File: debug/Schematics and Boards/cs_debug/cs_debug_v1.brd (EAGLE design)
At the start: 38.1 x 44.5 mm, 186 parts, among them J1 J-JTAG-CORTEX_SMD, J19 Solar, J2 J-JTAG-CORTEX_SMD, J3 J-JTAG-CORTEX-NEEDLE6-LEGS, J4 J-SERIAL-PORT, J5 J-WURTH-USBC, Q10 2N7002P, Q3 FDN340P, Q4 2N7002P, Q5 FDN340P, Q6 2N7002P, Q7 FDN340P, Q8 2N7002P, Q9 FDN340P, U1 AP2120N-3.3TRG1, U10 OPA357AIDBVTG4, U11 DAC7574IDGS, U12 MCP73871T-2CCI/ML, U13 USB2412-DZK, U2 TLV1117LV33DCYR, U3 INA225AIDGK, U4 OPA357AIDBVTG4, U5 INA225AIDGK, U6 OPA357AIDBVTG4, U7 INA225AIDGK, U8 OPA357AIDBVTG4, U9 INA225AIDGK, Y1 HCM49-24.000MABJ-UT, Y101 32.768kHz, Y102 12mHz-12pF-K7

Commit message: Add and name test points for debug board
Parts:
- removed C4: 68p, Capacitors:C0402
- removed C5, C6: 0.1u, Capacitors:C0402
- removed R10, R12, R14: 10k, Resistors:R0402
- removed R11: 100k, Resistors:R0402
- removed R13, R9: 249k, Resistors:R0402
- removed R15: 5.1, Resistors:R0603
- removed U3: INA225AIDGK, Amplifiers:DGK-MSOP8_INA225
- removed U4: OPA357AIDBVTG4, Amplifiers:OPA357AIDBVTG4
- added C20: 680pF, Capacitors:C0402
- added C21, C45: 0.1u, Capacitors:C0402
- added R53, R55, R57: 10k, Resistors:R0402
- added R54: 100k, Resistors:R0402
- added R56: 249k, Resistors:R0402
- added R58, R59: 5.1, Resistors:R0603
- added TP_3V3_IPROC, TP_3V3_MEAS, TP_M_D_DA_VO, TP_M_D_OA_EN, TP_M_D_OA_N, TP_M_D_OA_P, TP_M_D_OA_VO, TP_M_D_SDN, TP_M_D_VN, TP_M_D_VOI, TP_M_P_DA_VO, TP_M_P_OA_N, TP_M_P_OA_P, TP_M_P_OA_VO, TP_M_P_SDN, TP_M_P_VN, TP_M_P_VOI, TP_M_S_DA_VO, TP_M_S_OA_EN, TP_M_S_OA_N, TP_M_S_OA_P, TP_M_S_OA_VO, TP_M_S_SDN, TP_M_S_VN, TP_M_S_VOI, TP_M_T_DA_VO, TP_M_T_OA_EN, TP_M_T_OA_N, TP_M_T_OA_P, TP_M_T_OA_VO, TP_M_T_SDN, TP_M_T_VN, TP_M_T_VOI, TP_SCL, TP_SDA, T_M_P_OA_EN: TPTP10SQ, TestPoints:TP10SQ
- added U14: INA225AIDGK, Amplifiers:DGK-MSOP8_INA225
- added U15: OPA357AIDBVTG4, Amplifiers:OPA357AIDBVTG4
- C10, C13, C7: value 68p -> 680pF
- R16, R24, R40: value 5.1 -> 249k; device Resistors:R0603 -> Resistors:R0402
- R17, R21, R33, R37: value 249k -> 10k
- R18, R34: value 10k -> 100k
- R19, R35: value 100k -> 10k
- R20, R36: value 10k -> 249k
- R22, R38: value 10k -> 5.1; device Resistors:R0402 -> Resistors:R0603
- moved Q3 134.9 mm to (88.9, -91.4), turned to 180 degrees
- moved R16 126.5 mm to (96.5, -90.8), turned to 180 degrees
- moved Q4 125.1 mm to (88.9, -86.4), turned to 270 degrees
- moved Q7 88.0 mm to (88.9, -67.3), turned to 180 degrees
- moved R31 85.9 mm to (101.6, -67.3)
- moved U7 85.8 mm to (101.6, -62.2), turned to 270 degrees
- moved U5 85.2 mm to (101.6, -86.4), turned to 270 degrees
- moved R22 80.1 mm to (101.6, -91.4)
- moved C10 80.0 mm to (105.4, -62.2), turned to 90 degrees
- moved R25 79.6 mm to (96.5, -66.7), turned to 180 degrees
- moved C7 79.4 mm to (105.4, -86.4), turned to 90 degrees
- moved Q8 78.5 mm to (88.9, -62.2), turned to 270 degrees
- moved U8 78.5 mm to (94.0, -63.5), turned to 90 degrees
- moved U6 78.0 mm to (94.0, -87.6), turned to 90 degrees
- moved R17 77.8 mm to (94.0, -90.8)
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- renumbered JP11 to JP_VREG_SEL
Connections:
- net CM_DTR_DIFFAMP_N3 renamed CM_DIFFAMP_N3
- net CM_DTR_DIFFAMP_P3 renamed CM_DIFFAMP_P3
- removed net CM_DTR_OPAMP_ENABLE3: Q7.G, Q8.D, R27.1, U8.ENABLE
- removed net CM_DTR_OPAMP_N3: R28.1, R29.2, U8.IN-
- removed net CM_DTR_OPAMP_OUT3: Q7.S, R28.2, R31.1, U8.OUT
- removed net CM_DTR_OPAMP_P3: R25.2, R26.2, U8.IN+
- removed net CM_PROC_DIFFAMP_N1: C4.1, R15.2, U3.IN-
- removed net CM_PROC_DIFFAMP_P1: C4.2, R16.2, U3.IN+
- removed net CM_PROC_OPAMP_ENABLE1: Q3.G, Q4.D, R11.1, U4.ENABLE
- removed net CM_PROC_OPAMP_N1: R12.1, R13.2, U4.IN-
- removed net CM_PROC_OPAMP_OUT1: Q3.S, R12.2, R15.1, U4.OUT
- removed net CM_STORAGE_DIFFAMP_N1: C7.1, R23.2, U5.IN-
- removed net CM_STORAGE_DIFFAMP_P1: C7.2, R24.2, U5.IN+
- removed net CM_STORAGE_OPAMP_ENABLE1: Q5.G, Q6.D, R19.1, U6.ENABLE
- removed net CM_STORAGE_OPAMP_N1: R20.1, R21.2, U6.IN-
- removed net CM_STORAGE_OPAMP_OUT1: Q5.S, R20.2, R23.1, U6.OUT
- removed net CM_STORAGE_OPAMP_P1: R17.2, R18.2, U6.IN+
- removed net CM_TEMP_DIFFAMP_N1: C13.1, R39.2, U9.IN-
- removed net CM_TEMP_DIFFAMP_P1: C13.2, R40.2, U9.IN+
- removed net CM_TEMP_OPAMP_ENABLE1: Q10.D, Q9.G, R35.1, U10.ENABLE
- removed net CM_TEMP_OPAMP_N1: R36.1, R37.2, U10.IN-
- removed net CM_TEMP_OPAMP_OUT1: Q9.S, R36.2, R39.1, U10.OUT
- removed net CM_TEMP_OPAMP_P1: R33.2, R34.2, U10.IN+
- removed net CM__PROCOPAMP_P1: R10.2, R9.2, U4.IN+
- new net CM_DIFFAMP_N1: C20.1, R58.2, U14.IN-
- new net CM_DIFFAMP_N2: C13.1, R38.2, U9.IN-
- new net CM_DIFFAMP_N4: C7.1, R22.2, U5.IN-
- new net CM_DIFFAMP_P1: C20.2, R59.2, U14.IN+
- new net CM_DIFFAMP_P2: C13.2, R39.2, U9.IN+
- new net CM_DIFFAMP_P4: C7.2, R23.2, U5.IN+
- new net CM_OPAMP_ENABLE1: Q10.D, Q9.G, R54.1, TP_M_T_OA_EN.TP, U15.ENABLE
- new net CM_OPAMP_ENABLE2: Q5.G, Q6.D, R34.1, TP_M_S_OA_EN.TP, U10.ENABLE
- new net CM_OPAMP_ENABLE3: Q7.G, Q8.D, R27.1, TP_M_D_OA_EN.TP, U8.ENABLE
- new net CM_OPAMP_ENABLE4: Q3.G, Q4.D, R18.1, T_M_P_OA_EN.TP, U6.ENABLE
- new net CM_OPAMP_N1: R55.1, R56.2, TP_M_T_OA_N.TP, U15.IN-
- new net CM_OPAMP_N2: R35.1, R36.2, TP_M_S_OA_N.TP, U10.IN-
- new net CM_OPAMP_N3: R28.1, R29.2, TP_M_D_OA_N.TP, U8.IN-
- new net CM_OPAMP_N4: R19.1, R20.2, TP_M_P_OA_N.TP, U6.IN-
- new net CM_OPAMP_OUT1: Q9.S, R55.2, R58.1, TP_M_T_OA_VO.TP, U15.OUT
- new net CM_OPAMP_OUT2: Q5.S, R35.2, R38.1, TP_M_S_OA_VO.TP, U10.OUT
- new net CM_OPAMP_OUT3: Q7.S, R28.2, R31.1, TP_M_D_OA_VO.TP, U8.OUT
- new net CM_OPAMP_OUT4: Q3.S, R19.2, R22.1, TP_M_P_OA_VO.TP, U6.OUT
- new net CM_OPAMP_P1: R40.2, R53.2, TP_M_T_OA_P.TP, U15.IN+
- new net CM_OPAMP_P2: R24.2, R33.2, TP_M_S_OA_P.TP, U10.IN+
- new net CM_OPAMP_P3: R25.2, R26.2, TP_M_D_OA_P.TP, U8.IN+
- new net CM_OPAMP_P4: R16.2, R17.2, TP_M_P_OA_P.TP, U6.IN+
- net 3V3_INSTR_MEAS: now also C21.1, C45.1, R18.2, R21.2, R34.2, R37.2, R54.2, R57.2, TP_3V3_MEAS.TP, U14.VS, U15.VREF+; no longer C5.1, C6.1, R11.2, R14.2, R19.2, R22.2, R35.2, R38.2, U3.VS, U4.VREF+
- net 3V3_INSTR_PROC: now also TP_3V3_IPROC.TP
- net AGND: now also C21.2, C45.2, R20.1, R36.1, R56.1, U14.GND, U14.REF, U15.VREF-; no longer C5.2, C6.2, R13.1, R21.1, R37.1, U3.GND, U3.REF, U4.VREF-
- net CM_DTR_DCBIAS_SHUTDOWN: now also TP_M_D_SDN.TP
- net CM_DTR_DIFFAMP_OUT: now also TP_M_D_DA_VO.TP
- net CM_DTR_V_OFFSET_IN: now also TP_M_D_VOI.TP
- net CM_DTR_V_SENSE_N: now also TP_M_D_VN.TP
- net CM_PROC_DCBIAS_SHUTDOWN: now also R21.1, TP_M_P_SDN.TP; no longer R14.1
- net CM_PROC_DIFFAMP_GAIN0: now also U5.GS0; no longer U3.GS0
- net CM_PROC_DIFFAMP_GAIN1: now also U5.GS1; no longer U3.GS1
- net CM_PROC_DIFFAMP_OUT: now also TP_M_P_DA_VO.TP, U5.OUT; no longer U3.OUT
- net CM_PROC_V_OFFSET_IN: now also R16.1, TP_M_P_VOI.TP; no longer R9.1
- net CM_PROC_V_SENSE_N: now also R17.1, TP_M_P_VN.TP; no longer R10.1
- net CM_PROC_V_SENSE_P: now also R23.1; no longer R16.1
- net CM_STORAGE_DCBIAS_SHUTDOWN: now also R37.1, TP_M_S_SDN.TP; no longer R22.1
- net CM_STORAGE_DIFFAMP_GAIN0: now also U9.GS0; no longer U5.GS0
- net CM_STORAGE_DIFFAMP_GAIN1: now also U9.GS1; no longer U5.GS1
- net CM_STORAGE_DIFFAMP_OUT: now also TP_M_S_DA_VO.TP, U9.OUT; no longer U5.OUT
- net CM_STORAGE_V_OFFSET_IN: now also R24.1, TP_M_S_VOI.TP; no longer R17.1
- net CM_STORAGE_V_SENSE_N: now also R33.1, TP_M_S_VN.TP; no longer R18.1
- net CM_STORAGE_V_SENSE_P: now also R39.1; no longer R24.1
- net CM_TEMP_DCBIAS_SHUTDOWN: now also R57.1, TP_M_T_SDN.TP; no longer R38.1
- net CM_TEMP_DIFFAMP_GAIN0: now also U14.GS0; no longer U9.GS0
- net CM_TEMP_DIFFAMP_GAIN1: now also U14.GS1; no longer U9.GS1
- net CM_TEMP_DIFFAMP_OUT: now also TP_M_T_DA_VO.TP, U14.OUT; no longer U9.OUT
- net CM_TEMP_V_OFFSET_IN: now also R40.1, TP_M_T_VOI.TP; no longer R33.1
- net CM_TEMP_V_SENSE_N: now also R53.1, TP_M_T_VN.TP; no longer R34.1
- net CM_TEMP_V_SENSE_P: now also R59.1; no longer R40.1
- net INSTR_PROC_I2C_SCL: now also TP_SCL.TP
- net INSTR_PROC_I2C_SDA: now also TP_SDA.TP

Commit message: Add backup micro-usb ports
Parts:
- removed JP12, JP13: JUMPER-SMT_2_NC_PASTE_NO-SILK, Connectors:SMT-JUMPER_2_NC_PASTE_NO-SILK
- removed JP14, JP15, JP16: JUMPER-SMT_2_NC_PASTE_NO-SILK, SparkFun-Jumpers:SMT-JUMPER_2_NC_PASTE_NO-SILK
- removed JP_VREG_SEL: JUMPER-SMT_3_1-NC_PASTE_NO-SILK, Connectors:SMT-JUMPER_3_1-NC_PASTE_NO-SILK
- removed TP_SCL, TP_SDA: TPTP10SQ, TestPoints:TP10SQ
- removed U$5: BGX50A, Diodes:SOT143_BGX50A
- added D2: BGX50A, Diodes:SOT143_BGX50A
- added JP.IP.RST, JP.UART.VCC: JUMPER-SMT_2_NC_PASTE_NO-SILK, Connectors:SMT-JUMPER_2_NC_PASTE_NO-SILK
- added JP.USB.DDN, JP.USB.DDP, JP.USB.MDN, JP.USB.MDP, JP.VREG.SEL: JUMPER-SMT_3_1-NC_PASTE_NO-SILK, Connectors:SMT-JUMPER_3_1-NC_PASTE_NO-SILK
- added JP.USB.USART, JP.USBC.VBUS, JP.VEXT: JUMPER-SMT_2_NC_PASTE_NO-SILK, SparkFun-Jumpers:SMT-JUMPER_2_NC_PASTE_NO-SILK
- added JP.USBM.DBG, JP.USBM.MAIN: JUMPER-SMT_2_NO_PASTEFREE, Connectors:SMT-JUMPER_2_NO_PASTEFREE_NO-SILK
- added J_USB_DBG, J_USB_MAIN: USBABSMTDIP, ZX62D-AB-5P8:ZX62D-AB-5P8
- added SCL, SDA: TPTP10SQ, TestPoints:TP10SQ
- added VR1, VR2, VR5, VR6, VR7, VR8: VARISTOR, Diodes:R0603
- C46: device Capacitors:C0805 -> Capacitors:C0603
- moved C46 298.0 mm to (47.0, -154.9)
- moved C47 298.0 mm to (38.7, -165.7)
- moved C48 298.0 mm to (19.7, -171.4)
- moved C49 298.0 mm to (19.7, -175.3)
- moved C50 298.0 mm to (19.7, -177.2)
- moved C51 298.0 mm to (19.7, -179.1)
- moved C52 298.0 mm to (19.7, -181.0)
- moved C53 298.0 mm to (19.7, -182.9)
- moved C54 298.0 mm to (19.7, -184.8)
- moved C55 298.0 mm to (20.3, -193.0)
- moved C56 298.0 mm to (20.3, -196.2)
- moved R42 298.0 mm to (50.8, -154.9)
- moved R43 298.0 mm to (54.6, -154.9)
- moved R44 298.0 mm to (38.7, -157.5)
- moved R45 298.0 mm to (38.7, -160.0)
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- renumbered JP1 to JP.P.PROC, JP101 to JP.IP.AREF, JP102 to JP.IP.VDDIO, JP103 to JP.IP.ANA, JP104 to JP.IP.UTMI, JP105 to JP.IP.OUT, JP106 to JP.IP.CORE, JP107 to JP.IP.PLL, JP2 to JP.P.STOR, JP3 to JP.P.TEMP, JP4 to JP.P.DTR, JP5 to JP.EN.VMEAS, JP6 to JP.EN.VPROC, JP7 to JP.VDD.MAIN, JP8 to JP.UART.TX.IP, JP9 to JP.UART.RX.IP, TP_M_D_DA_VO to M.D.DA.VO, TP_M_D_OA_EN to M.D.OA.EN, TP_M_D_OA_N to M.D.OA.N, TP_M_D_OA_P to M.D.OA.P, TP_M_D_OA_VO to M.D.OA.VO, TP_M_D_SDN to M.D.SDN, TP_M_D_VN to M.D.VN, TP_M_D_VOI to M.D.VOI, TP_M_P_DA_VO to M.P.DA.VO, TP_M_P_OA_N to M.P.OA.N, TP_M_P_OA_P to M.P.OA.P, TP_M_P_OA_VO to M.P.OA.VO, TP_M_P_SDN to M.P.SDN, TP_M_P_VN to M.P.VN, TP_M_P_VOI to M.P.VOI, TP_M_S_DA_VO to M.S.DA.VO, TP_M_S_OA_EN to M.S.OA.EN, TP_M_S_OA_N to M.S.OA.N, TP_M_S_OA_P to M.S.OA.P, TP_M_S_OA_VO to M.S.OA.VO, TP_M_S_SDN to M.S.SDN, TP_M_S_VN to M.S.VN, TP_M_S_VOI to M.S.VOI, TP_M_T_DA_VO to M.T.DA.VO, TP_M_T_OA_EN to M.T.OA.EN, TP_M_T_OA_N to M.T.OA.N, TP_M_T_OA_P to M.T.OA.P, TP_M_T_OA_VO to M.T.OA.VO, TP_M_T_SDN to M.T.SDN, TP_M_T_VN to M.T.VN, TP_M_T_VOI to M.T.VOI, T_M_P_OA_EN to M.P.OA.EN
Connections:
- new net HUB_INSTR_PROC_USB_D_N: JP.USB.DDN.3, U13.2
- new net HUB_INSTR_PROC_USB_D_P: JP.USB.DDP.3, U13.3
- new net HUB_MAIN_USB_DATA_N: U13.28
- new net HUB_MAIN_USB_DATA_P: JP.USB.MDN.3, JP.USB.MDP.3, U13.1
- new net USB_BKUP_DBG_D_N: JP.USB.DDN.1, J_USB_DBG.D-, VR5.1
- new net USB_BKUP_DBG_D_P: JP.USB.DDP.1, J_USB_DBG.D+, VR2.1
- new net USB_BKUP_DBG_OTGID: J_USB_DBG.USBID, VR1.1
- new net USB_BKUP_DBG_VBUS: JP.USBM.DBG.2, J_USB_DBG.VBUS
- new net USB_BKUP_MAIN_D_N: JP.USB.MDP.1, J_USB_MAIN.D-, VR8.1
- new net USB_BKUP_MAIN_D_P: JP.USB.MDN.1, J_USB_MAIN.D+, VR7.1
- new net USB_BKUP_MAIN_OTGID: J_USB_MAIN.USBID, VR6.1
- new net USB_BKUP_MAIN_VBUS: JP.USBM.MAIN.2, J_USB_MAIN.VBUS
- net 3V3_INSTR_PROC: now also JP.UART.VCC.1; no longer JP13.1
- net DGND: now also D2.3; no longer U$5.3
- net GND: now also J_USB_DBG.GND, J_USB_DBG.S1, J_USB_DBG.S2, J_USB_DBG.S3, J_USB_DBG.S4, J_USB_MAIN.GND, J_USB_MAIN.S1, J_USB_MAIN.S2, J_USB_MAIN.S3, J_USB_MAIN.S4, VR1.2, VR2.2, VR5.2, VR6.2, VR7.2, VR8.2
- net INSTR_PROC_I2C_SCL: now also SCL.TP; no longer TP_SCL.TP
- net INSTR_PROC_I2C_SDA: now also SDA.TP; no longer TP_SDA.TP
- net INSTR_PROC_NRESET: now also JP.IP.RST.1; no longer JP12.1
- net INSTR_PROC_NRESET_SW: now also JP.IP.RST.2; no longer JP12.2
- net INSTR_PROC_USB_D_N: now also JP.USB.DDN.2; no longer U13.2
- net INSTR_PROC_USB_D_P: now also JP.USB.DDP.2; no longer U13.3
- net MAIN_USART_TX: now also JP.USB.USART.2; no longer JP16.2
- net MAIN_USB_DATA_N: now also JP.USB.MDN.2; no longer U13.28
- net MAIN_USB_DATA_P: now also JP.USB.MDP.2; no longer U13.1
- net N$11: now also JP.UART.VCC.2; no longer JP13.2
- net N$15: now also JP.VEXT.1; no longer JP14.1
- net UCTX_DBGRX: now also JP.USB.USART.1; no longer JP16.1
- net USB_CONN_D_N: now also D2.2; no longer U$5.2
- net USB_CONN_D_P: now also D2.4; no longer U$5.4
- net USB_VBUS: now also D2.1, JP.USBC.VBUS.1, JP.USBC.VBUS.2, JP.USBM.DBG.1, JP.USBM.MAIN.1, JP.VEXT.2; no longer JP14.2, JP15.1, JP15.2, U$5.1
- net VCHRG_OUT: now also JP.VREG.SEL.3; no longer JP_VREG_SEL.3
- net VREG_IN: now also JP.VREG.SEL.2; no longer JP_VREG_SEL.2
- net VSRC_RAW: now also JP.VREG.SEL.1; no longer JP_VREG_SEL.1

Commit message: Dbg board: subsystem organization
Did relative placement for all subsystems (processor, regulator, usb- hub, etc.)

It is unlikely that all components on this board can fit into a small footprint due to the size and number of components. Some further squeezing and optimization can be done, but part of the board will need to be larger to expose vertically accessed ports (debug).
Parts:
- removed JP.VEXT, JP10: JUMPER-SMT_2_NC_PASTE_NO-SILK, SparkFun-Jumpers:SMT-JUMPER_2_NC_PASTE_NO-SILK
- removed S1, S102: Momentary, Switches:SW_EVQ-P7L01P
- removed TP_3V3_IPROC, TP_3V3_MEAS: TPTP10SQ, TestPoints:TP10SQ
- added 3V3.IPROC, 3V3.MEAS: TPTP10SQ, TestPoints:TP10SQ
- added JP.CHRG.MAIN, JP.EXT.PWR, JP.UART.RX, JP.UART.TX: JUMPER-SMT_2_NC_PASTE_NO-SILK, Connectors:SMT-JUMPER_2_NC_PASTE_NO-SILK
- added S.ERASE, S.NRST: Momentary, Switches:SW_EVQ-P7L01P
- JP.EN.VMEAS, JP.EN.VPROC, JP.P.DTR, JP.P.PROC, JP.P.STOR, JP.P.TEMP, JP.USB.USART, JP.USBC.VBUS, JP.VDD.MAIN: device SparkFun-Jumpers:SMT-JUMPER_2_NC_PASTE_NO-SILK -> Connectors:SMT-JUMPER_2_NC_PASTE_NO-SILK
- Y1: value HCM49-24.000MABJ-UT -> EPSON_TSX-3225_24.0000MF10Z-C3; device Oscillators:XTAL_HCM49 -> Oscillators:XTAL_EPSON_TSX3225
- moved JP.USB.DDP 268.4 mm to (94.6, -135.3), turned to 90 degrees
- moved JP.USB.DDN 263.8 mm to (94.6, -130.2), turned to 90 degrees
- moved JP.USB.MDN 243.5 mm to (95.2, -150.5), turned to 90 degrees
- moved JP.USB.MDP 238.9 mm to (95.2, -145.4), turned to 90 degrees
- moved VR5 233.9 mm to (86.4, -130.2)
- moved JP.UART.VCC 231.0 mm to (-56.5, 36.8), turned to 180 degrees
- moved VR2 230.4 mm to (86.4, -132.1)
- moved VR8 229.5 mm to (85.7, -145.4)
- moved VR1 226.9 mm to (86.4, -134.0)
- moved JP.USBM.DBG 226.8 mm to (82.5, -127.6), turned to 270 degrees
- moved VR7 226.0 mm to (85.7, -147.3)
- moved J4 222.9 mm to (-64.8, 37.5)
- moved VR6 222.6 mm to (85.7, -149.2)
- moved JP.USBM.MAIN 215.3 mm to (83.2, -142.2), turned to 180 degrees
- moved J1 202.3 mm to (54.6, 54.0)
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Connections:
- removed net GND: C18.2, C208.2, J19.2, J_USB_DBG.GND, J_USB_DBG.S1, J_USB_DBG.S2, J_USB_DBG.S3, J_USB_DBG.S4, J_USB_MAIN.GND, J_USB_MAIN.S1, J_USB_MAIN.S2, J_USB_MAIN.S3, J_USB_MAIN.S4, S1.1_1, S1.1_2, VR1.2, VR2.2, VR5.2, VR6.2, VR7.2, VR8.2
- removed net N$12: U13.15, U13.6
- new net N$7: J4.4, JP.UART.TX.2
- new net N$9: J4.5, JP.UART.RX.2
- new net VSRC: JP.EXT.PWR.2, JP.USBC.VBUS.2, JP.USBM.DBG.1, JP.USBM.MAIN.1, L1.1
- net 3V3_INSTR_MEAS: now also 3V3.MEAS.TP; no longer TP_3V3_MEAS.TP
- net 3V3_INSTR_PROC: now also 3V3.IPROC.TP, S.ERASE.1_1, S.ERASE.1_2; no longer S102.1_1, S102.1_2, TP_3V3_IPROC.TP
- net DGND: now also C18.2, C208.2, J19.2, J_USB_DBG.GND, J_USB_DBG.S1, J_USB_DBG.S2, J_USB_DBG.S3, J_USB_DBG.S4, J_USB_MAIN.GND, J_USB_MAIN.S1, J_USB_MAIN.S2, J_USB_MAIN.S3, J_USB_MAIN.S4, S.NRST.1_1, S.NRST.1_2, U13.15, U13.6, VR1.2, VR2.2, VR5.2, VR6.2, VR7.2, VR8.2, Y1.2, Y1.4
- net ERASE_S: now also S.ERASE.2_1, S.ERASE.2_2; no longer S102.2_1, S102.2_2
- net HUB_MAIN_USB_DATA_N: now also JP.USB.MDN.3
- net HUB_MAIN_USB_DATA_P: no longer JP.USB.MDN.3
- net INSTR_PROC_NRESET_SW: now also S.NRST.2_1, S.NRST.2_2; no longer S1.2_1, S1.2_2
- net MAIN_USART_RX: now also JP.UART.RX.1; no longer J4.5
- net MAIN_USART_TX: now also JP.UART.TX.1; no longer J4.4
- net N$15: now also JP.EXT.PWR.1; no longer JP.VEXT.1
- net N$21: now also Y1.3; no longer Y1.2
- net USB_VBUS: no longer JP.USBC.VBUS.2, JP.USBM.DBG.1, JP.USBM.MAIN.1, JP.VEXT.2, L1.1
- net VCHRG_BATT: now also JP.CHRG.MAIN.1; no longer JP10.1
- net V_BATT_MAIN: now also JP.CHRG.MAIN.2; no longer JP10.2

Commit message: Relative subsystem placement
still off board
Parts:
- added JP.USB.VBUSP: JUMPER-SMT_3_1-NC_PASTE_NO-SILK, Connectors:SMT-JUMPER_3_1-NC_PASTE_NO-SILK
- moved R49 286.8 mm to (-61.0, 78.1), turned to 180 degrees
- moved R50 286.3 mm to (-59.1, 77.3), turned to 270 degrees
- moved C48 285.0 mm to (-61.0, 76.8), turned to 180 degrees
- moved R51 284.9 mm to (-62.8, 77.2), turned to 90 degrees
- moved C52 284.8 mm to (-57.1, 75.6), turned to 0 degrees
- moved C53 284.4 mm to (-64.1, 77.2), turned to 90 degrees
- moved R52 282.2 mm to (-57.1, 73.7), turned to 180 degrees
- moved C56 281.6 mm to (-70.3, 73.9)
- moved R44 279.6 mm to (-57.1, 71.8), turned to 0 degrees
- moved C51 277.9 mm to (-57.1, 70.5), turned to 0 degrees
- moved U13 277.9 mm to (-61.6, 71.8), turned to 90 degrees
- moved Y1 277.4 mm to (-67.9, 73.0), turned to 90 degrees
- moved C55 275.9 mm to (-70.3, 71.8)
- moved R48 273.1 mm to (-66.0, 69.2), turned to 90 degrees
- moved R45 271.9 mm to (-58.6, 66.5), turned to 180 degrees
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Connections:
- removed net USB_VBUS: C46.1, C47.1, D2.1, J5.A4, J5.A9, J5.B4, J5.B9, JP.USBC.VBUS.1, R47.2, U_INSTR_PROC.39
- new net USBC_VBUS: C46.1, C47.1, D2.1, J5.A4, J5.A9, J5.B4, J5.B9, JP.USB.VBUSP.3, JP.USBC.VBUS.1, R47.2
- new net USB_VBUS_IPROC: JP.USB.VBUSP.2, U_INSTR_PROC.39
- net USB_BKUP_DBG_VBUS: now also JP.USB.VBUSP.1

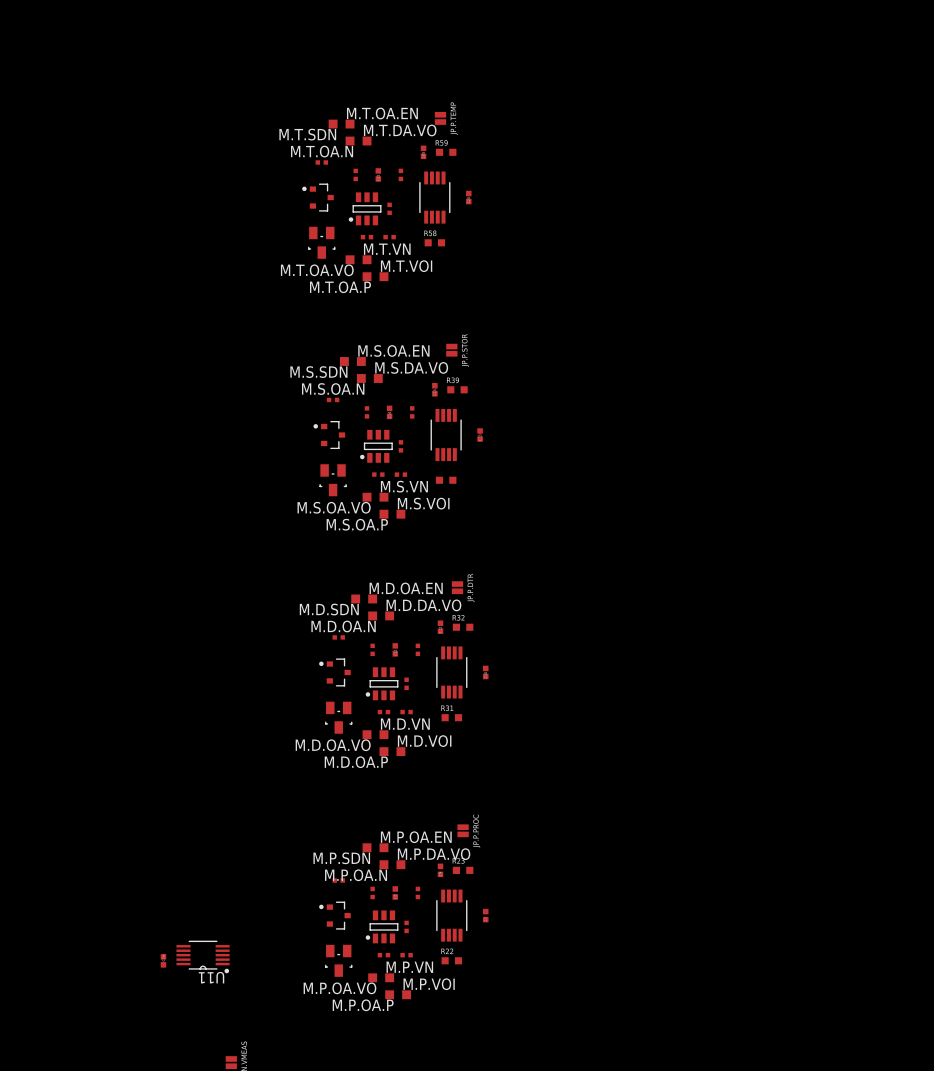
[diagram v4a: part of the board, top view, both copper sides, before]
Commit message: DBG- begin board placement and routing
Will create another branch for the many commits needed as part of routing
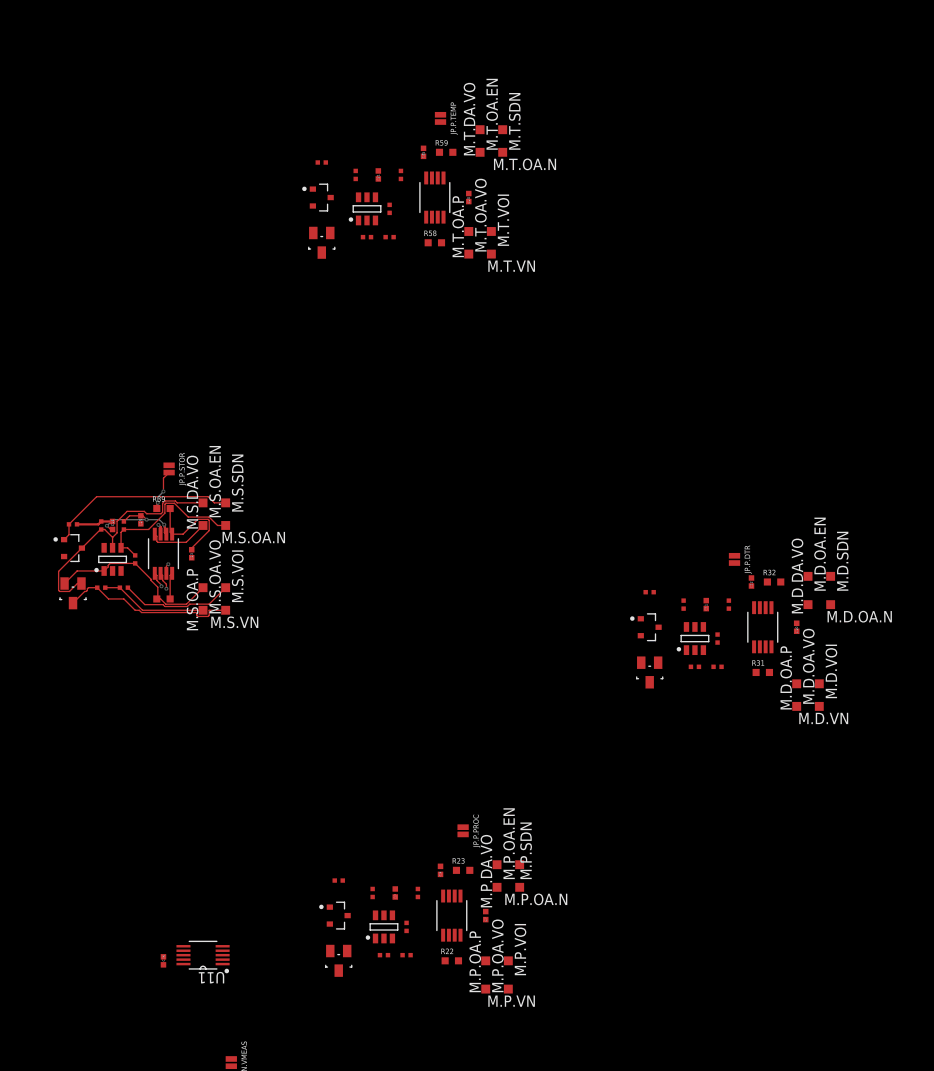
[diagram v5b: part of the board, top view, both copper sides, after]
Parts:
- moved M.D.SDN 53.4 mm to (162.6, 25.4), turned to 270 degrees
- moved M.D.OA.N 51.5 mm to (162.6, 22.2)
- moved M.D.VN 49.0 mm to (161.3, 10.8), turned to 180 degrees
- moved M.D.OA.EN 49.0 mm to (160.0, 25.4), turned to 270 degrees
- moved M.D.OA.VO 48.6 mm to (158.8, 13.3), turned to 270 degrees
- moved M.D.VOI 47.6 mm to (161.3, 13.3), turned to 270 degrees
- moved M.D.DA.VO 47.0 mm to (160.0, 22.2), turned to 270 degrees
- moved M.D.OA.P 46.6 mm to (158.8, 10.8), turned to 90 degrees
- moved C15 36.1 mm to (85.1, 31.8)
- moved R39 35.6 mm to (87.6, 33.0)
- moved Q7 35.3 mm to (142.2, 14.6)
- moved Q8 35.3 mm to (142.2, 19.7)
- moved R25 35.3 mm to (149.9, 15.2)
- moved R27 35.3 mm to (146.1, 22.2)
- moved R28 35.3 mm to (149.9, 18.4)
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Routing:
- net CM_OPAMP_ENABLE2: track 0.00 -> 28.2 mm
- net CM_STORAGE_DCBIAS_SHUTDOWN: track 0.00 -> 21.1 mm
- net CM_OPAMP_OUT2: track 0.00 -> 20.2 mm
- net CM_STORAGE_V_SENSE_N: track 0.00 -> 20.1 mm
- net CM_OPAMP_N2: track 0.00 -> 18.4 mm
- net AGND: track 0.00 -> 13.0 mm, vias 0 -> 4
- net CM_STORAGE_V_OFFSET_IN: track 0.00 -> 12.7 mm
- net CM_OPAMP_P2: track 0.00 -> 12.0 mm
- net CM_DIFFAMP_P2: track 0.00 -> 12.0 mm
- net CM_STORAGE_DIFFAMP_OUT: track 0.00 -> 6.92 mm
- net 3V3_INSTR_MEAS: track 0.00 -> 5.27 mm, vias 0 -> 1
- net CM_STORAGE_V_SENSE_P: track 0.00 -> 4.61 mm, vias 0 -> 2
- net CM_DIFFAMP_N2: track 0.00 -> 2.97 mm
- net CM_STORAGE_DIFFAMP_GAIN1: track 0.00 -> 2.00 mm, vias 0 -> 1
- net CM_STORAGE_DIFFAMP_GAIN0: track 0.00 -> 1.77 mm, vias 0 -> 1
